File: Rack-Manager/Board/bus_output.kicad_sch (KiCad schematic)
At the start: 8 parts, among them J3 Conn_01x03_Pin, M1 Fan_4pin, U10 DMG6601

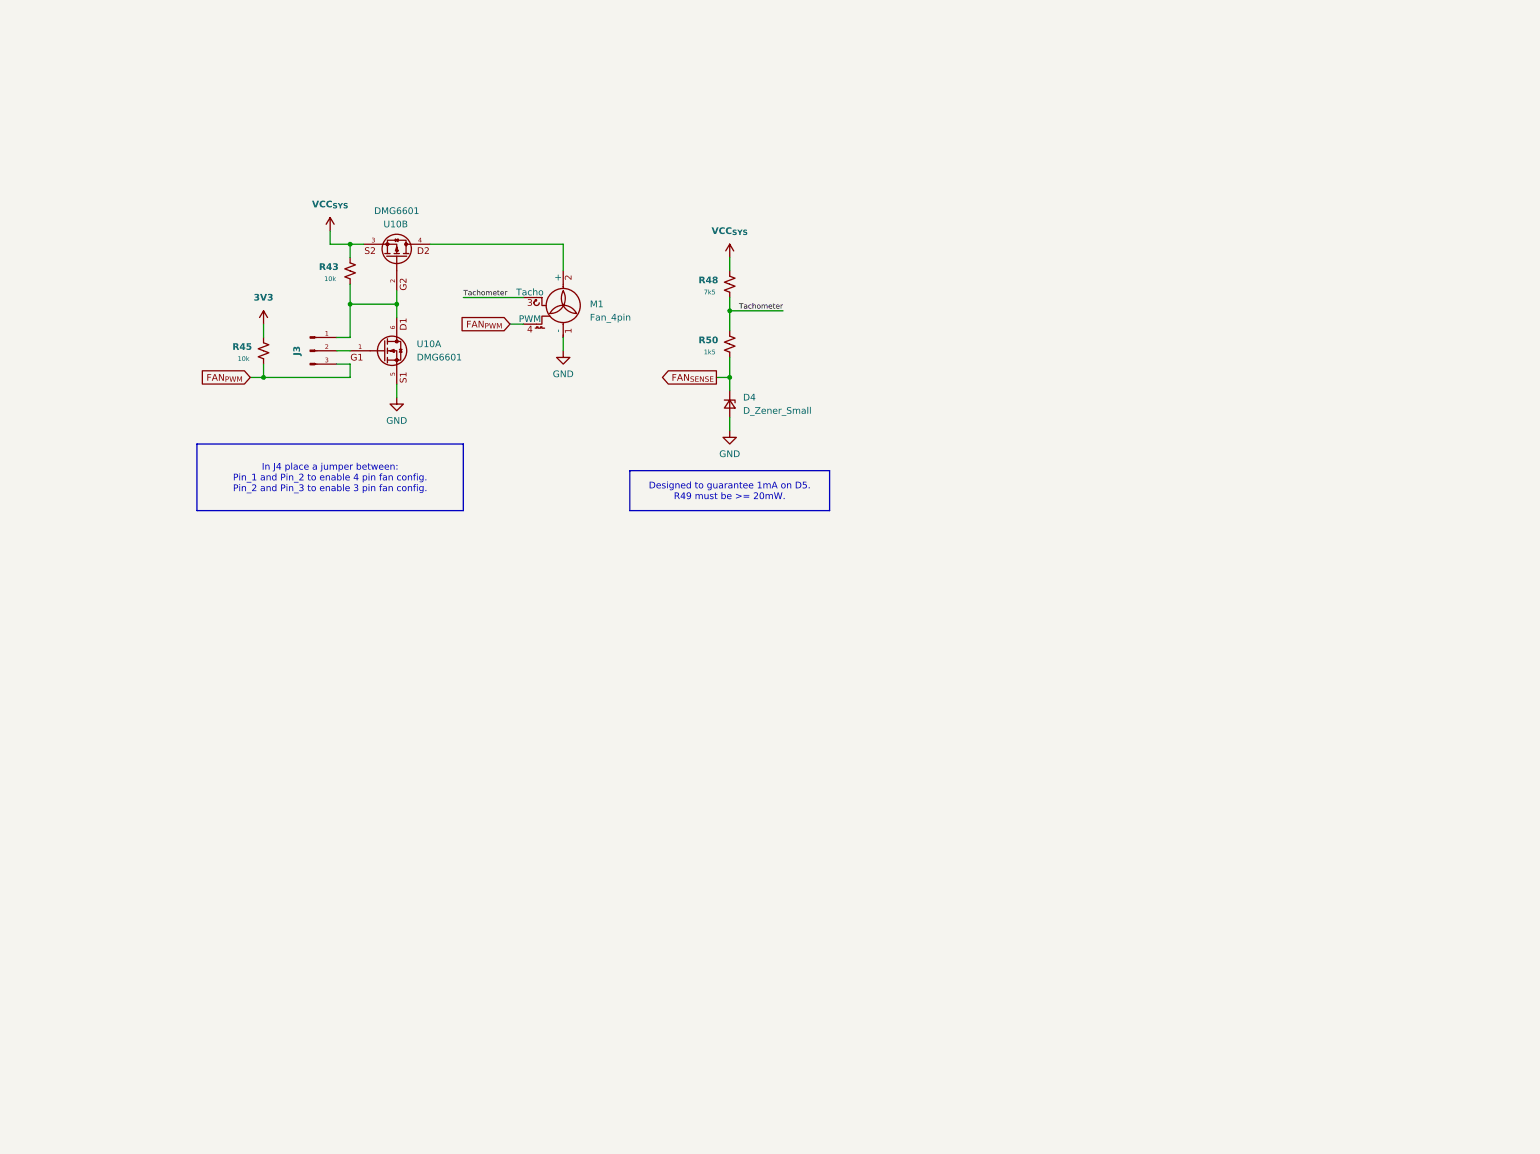
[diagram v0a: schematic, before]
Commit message: Fixed FAN control link mixed with bus output file
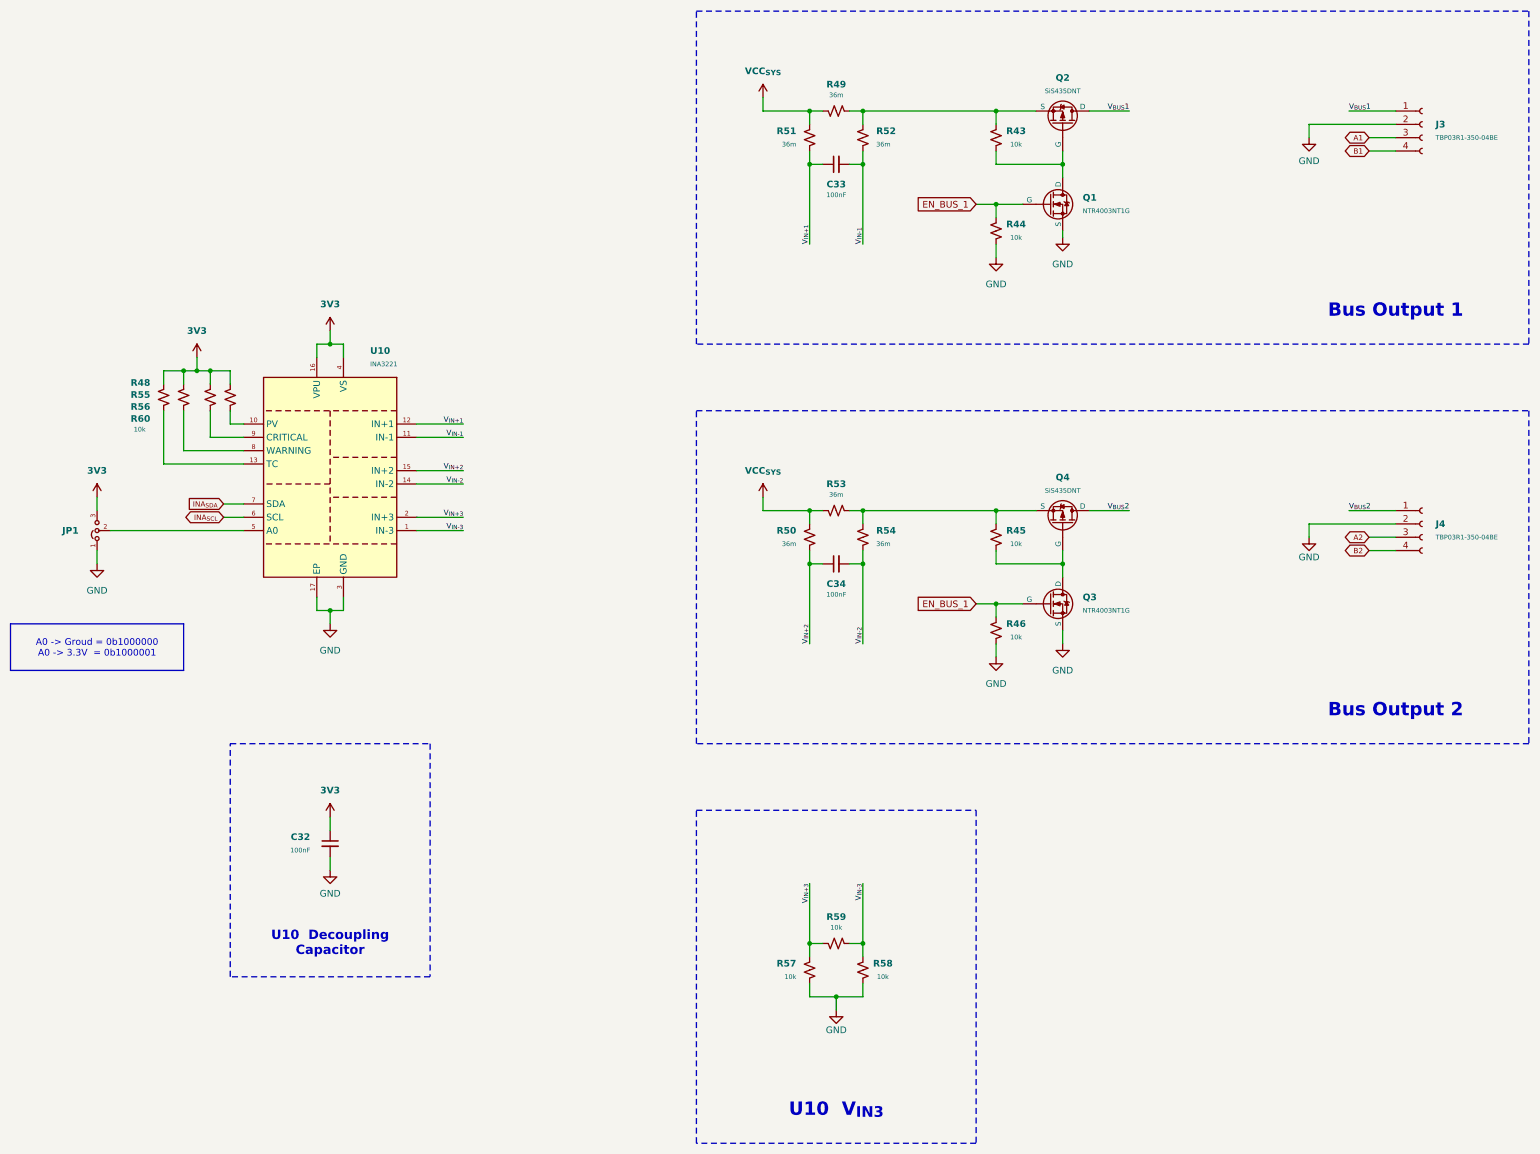
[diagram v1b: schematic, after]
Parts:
- removed D4: D_Zener_Small, Diode_SMD:D_SOD-123, symbol Device:D_Zener_Small
- removed J3: Conn_01x03_Pin, Connector_PinSocket_2.54mm:PinSocket_1x03_P2.54mm_Vertical, symbol Connector:Conn_01x03_Pin
- removed M1: Fan_4pin, Connector:FanPinHeader_1x04_P2.54mm_Vertical, symbol Motor:Fan_4pin
- removed U10: DMG6601, symbol Diodes:DMG6601
- added C32, C33, C34: 100nF, Capacitor_SMD:C_0402_1005Metric, symbol Device:C_Small
- added J3, J4: TBP03R1-350-04BE, Same Sky:TBP03R1-350-04BE, symbol Connector:Conn_01x04_Socket
- added JP1: Jumper_3_Bridged12, TestPoint:TestPoint_2Pads_Pitch5.08mm_Drill1.3mm, symbol Jumper:Jumper_3_Bridged12
- added Q1, Q3: NTR4003NT1G, Package_TO_SOT_SMD:SOT-23-3, symbol Simulation_SPICE:NMOS
- added Q2, Q4: SiS435DNT, symbol Simulation_SPICE:PMOS
- added R44, R46, R55, R56, R57, R58, R60: 10k, Resistor_SMD:R_0201_0603Metric, symbol Device:R_Small_US
- added R49, R51, R52, R53, R54: 36m, symbol Device:R_Small_US
- added R59: 10k, Resistor_SMD:R_0402_1005Metric, symbol Device:R_Small_US
- added U10: INA3221, Package_DFN_QFN:Texas_RGV0016A_VQFN-16-1EP_4x4mm_P0.65mm_EP2.1x2.1mm, symbol Power_Management:INA3221
- R43, R45: footprint Resistor_SMD:R_0402_1005Metric -> Resistor_SMD:R_0201_0603Metric
- R48: value 7k5 -> 10k; footprint Resistor_SMD:R_0402_1005Metric -> Resistor_SMD:R_0201_0603Metric
- R50: value 1k5 -> 36m; footprint Resistor_SMD:R_0402_1005Metric -> (none); JLCPCB # (none) -> LTR18EZPFSR036; Manufacturer (none) -> ROhm; Model (none) -> LTR18EZPFSR036; Mouser Link (none) -> https://eu.mouser.com/ProductDetail/755-LTR18EZPFSR036
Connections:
- net 3V3: now also R48.2, C32.1, JP1.3 (B), R55.2, R56.2, R60.2, U10.16 (VPU), U10.4 (VS); no longer R45.2
- net GND: now also C32.2, J3.2 (Pin_2), J4.2 (Pin_2), JP1.1 (A), Q1.2 (S), Q3.2 (S), R44.1, R46.1, R57.1, R58.1, U10.17 (EP), U10.3 (GND)
- net VCC_{SYS}: now also R50.2, R49.2, R51.2, R53.2; no longer R43.2, R48.2
- net at R43.1: now also Q1.3 (D), Q2.2 (G)
- net FAN_{PWM}: no longer names the net of R45.1
- net FAN_{PWM}: now also Q3.3 (D), Q4.2 (G)
- net FAN_{SENSE} renamed V_{IN+2}
- net V_{IN+2}: now also C34.1, U10.15 (IN+2)
- net Tachometer: no longer names the net of R48.1
- net Tachometer: now also U10.10 (PV); no longer R50.2
- new net: Q2.1 (S), R43.2, R49.1, R52.2
- new net: Q4.1 (S), R45.2, R53.1, R54.2
- new net: JP1.2 (C), U10.5 (A0)
- new net: R56.1, U10.8 (WARNING)
- new net: R60.1, U10.13 (TC)
- new net: R55.1, U10.9 (CRITICAL)
- new net A1: J3.3 (Pin_3)
- new net A2: J4.3 (Pin_3)
- new net B1: J3.4 (Pin_4)
- new net B2: J4.4 (Pin_4)
- new net EN_BUS_1: Q1.1 (G), Q3.1 (G), R44.2, R46.2
- new net INA_{SCL}: U10.6 (SCL)
- new net INA_{SDA}: U10.7 (SDA)
- new net V_{BUS}1: J3.1 (Pin_1), Q2.3 (D)
- new net V_{BUS}2: J4.1 (Pin_1), Q4.3 (D)
- new net V_{IN+1}: C33.1, R51.1, U10.12 (IN+1)
- new net V_{IN+3}: R57.2, R59.1, U10.2 (IN+3)
- new net V_{IN-1}: C33.2, R52.1, U10.11 (IN-1)
- new net V_{IN-2}: C34.2, R54.1, U10.14 (IN-2)
- new net V_{IN-3}: R58.2, R59.2, U10.1 (IN-3)
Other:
- note added: "Bus Output 1"
- note added: "Bus Output 2"
- note added: "U10 Decoupling Capacitor"
- note added: "U10 V_{IN3}"

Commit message: Added RS485 protection data as task describe and fixed stuff around
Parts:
- JP1: footprint TestPoint:TestPoint_2Pads_Pitch5.08mm_Drill1.3mm -> Jumper:SolderJumper-3_P1.3mm_Bridged12_RoundedPad1.0x1.5mm
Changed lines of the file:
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@@
 			)
 		)
-		(property "Footprint" "TestPoint:TestPoint_2Pads_Pitch5.08mm_Drill1.3mm"
+		(property "Footprint" "Jumper:SolderJumper-3_P1.3mm_Bridged12_RoundedPad1.0x1.5mm"
 			(at 54.61 130.81 0)
 			(effects

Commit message: Fixed volteage divider for fan tachometer and fixed other pull-x and divider for the microcontroller
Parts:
- R43, R45: value 10k -> 100k
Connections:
- net EN_BUS_1: no longer Q3.1 (G), R46.2
- new net EN_BUS_2: Q3.1 (G), R46.2
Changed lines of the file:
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@@
 		)
 	)
-	(global_label "EN_BUS_1"
+	(global_label "EN_BUS_2"
 		(shape input)
 		(at 237.49 144.78 180)
@@
 		)
 		(property "Intersheetrefs" "${INTERSHEET_REFS}"
-			(at 223.9593 144.78 0)
+			(at 225.0706 144.78 0)
 			(effects
 				(font
@@
 			)
 		)
-		(property "Value" "10k"
+		(property "Value" "100k"
 			(at 245.11 133.35 0)
 			(effects
@@
 			)
 		)
-		(property "Value" "10k"
+		(property "Value" "100k"
 			(at 245.11 57.15 0)
 			(effects
